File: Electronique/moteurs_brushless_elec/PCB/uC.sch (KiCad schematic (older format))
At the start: 17 parts, among them J1 CONN_SERIAL, J2 swdio, P1 CONN_I2C, P2 CONN_FREE, P3 CONN_CAN, U3 stm32f303k8t6, U9 MCP2562, Y1 Crystal_8MHz

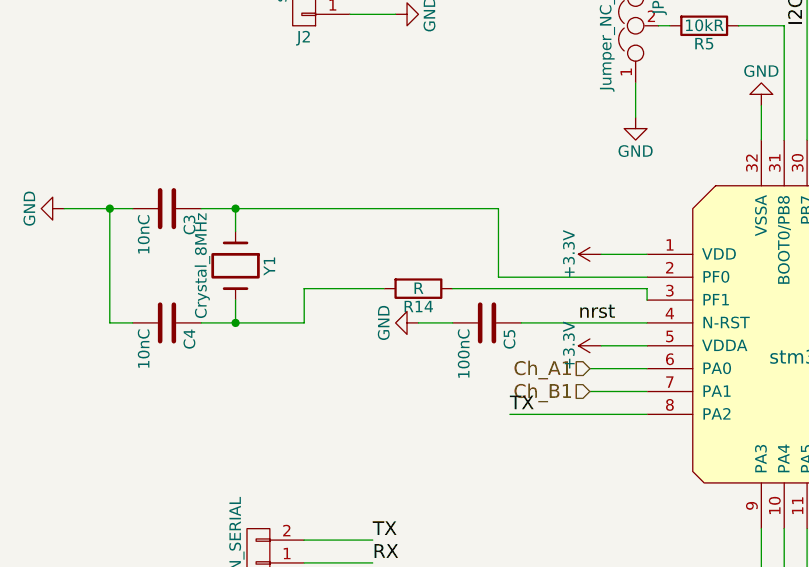
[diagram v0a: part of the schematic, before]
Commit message: pas de place pour le quartz
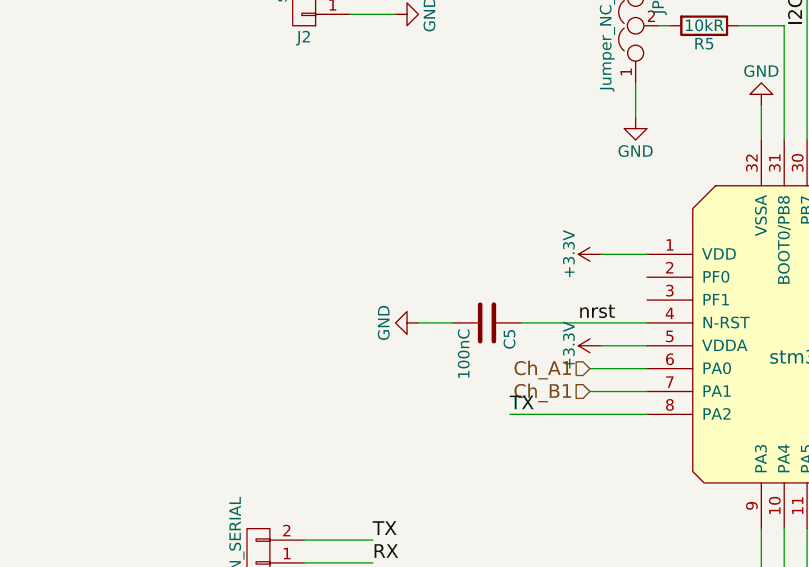
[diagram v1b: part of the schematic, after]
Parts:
- removed C3, C4: 10nC, Capacitors_SMD:C_1206_HandSoldering, symbol C
- removed R14: R, Resistors_SMD:R_1206_HandSoldering, symbol R
- removed Y1: Crystal_8MHz, Crystals:Crystal_HC49-4H_Vertical, symbol Crystal
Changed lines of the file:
@@
 I2C_SCL
-$Comp
-L Crystal Y1
-U 1 1 59C158A8
-P 3150 2750
-F 0 "Y1" H 3150 2900 50  0000 C CNN
-F 1 "Crystal_8MHz" H 3150 2600 50  0000 C CNN
-F 2 "Crystals:Crystal_HC49-4H_Vertical" H 3150 2750 50  0001 C CNN
-F 3 "" H 3150 2750 50  0000 C CNN
-	1    3150 2750
-	0    1    1    0
-$EndComp
-$Comp
-L C C3
-U 1 1 59C15931
-P 2850 2500
-F 0 "C3" H 2875 2600 50  0000 L CNN
-F 1 "10nC" H 2875 2400 50  0000 L CNN
-F 2 "Capacitors_SMD:C_1206_HandSoldering" H 2888 2350 50  0001 C CNN
-F 3 "" H 2850 2500 50  0000 C CNN
-	1    2850 2500
-	0    1    1    0
-$EndComp
-$Comp
-L C C4
-U 1 1 59C15C12
-P 2850 3000
-F 0 "C4" H 2875 3100 50  0000 L CNN
-F 1 "10nC" H 2875 2900 50  0000 L CNN
-F 2 "Capacitors_SMD:C_1206_HandSoldering" H 2888 2850 50  0001 C CNN
-F 3 "" H 2850 3000 50  0000 C CNN
-	1    2850 3000
-	0    1    1    0
-$EndComp
-$Comp
-L GND #PWR038
-U 1 1 59C15C7D
-P 2400 2500
-F 0 "#PWR038" H 2400 2250 50  0001 C CNN
-F 1 "GND" H 2400 2350 50  0000 C CNN
-F 2 "" H 2400 2500 50  0000 C CNN
-F 3 "" H 2400 2500 50  0000 C CNN
-	1    2400 2500
-	0    1    1    0
-$EndComp
-Wire Wire Line
-	2400 2500 2700 2500
-Wire Wire Line
-	2700 3000 2600 3000
-Wire Wire Line
-	2600 3000 2600 2500
-Connection ~ 2600 2500
-Wire Wire Line
-	3000 2500 4300 2500
-Wire Wire Line
-	3150 2500 3150 2600
-Wire Wire Line
-	3000 3000 3450 3000
-Wire Wire Line
-	3150 3000 3150 2900
-Connection ~ 3150 2500
-Connection ~ 3150 3000
 $Comp
 L CONN_01X02 P2
@@
 	5650 3900 5650 4550
 $Comp
-L R R14
-U 1 1 59C17650
-P 3950 2850
-F 0 "R14" V 4030 2850 50  0000 C CNN
-F 1 "R" V 3950 2850 50  0000 C CNN
-F 2 "Resistors_SMD:R_1206_HandSoldering" V 3880 2850 50  0001 C CNN
-F 3 "" H 3950 2850 50  0000 C CNN
-	1    3950 2850
-	0    1    1    0
-$EndComp
-Wire Wire Line
-	4100 2850 4950 2850
-Wire Wire Line
-	4950 2850 4950 2900
-Wire Wire Line
-	3800 2850 3450 2850
-Wire Wire Line
-	3450 2850 3450 3000
-Wire Wire Line
-	4300 2500 4300 2800
-Wire Wire Line
-	4300 2800 4950 2800
-$Comp
 L MCP2562 U9

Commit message: correction
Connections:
- no-connect marks 0 -> 2
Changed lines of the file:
@@
 $EndComp
 $Comp
-L +3.3V #PWR039
+L +3.3V #PWR038
 U 1 1 59C2F346
 P 3300 4500
-F 0 "#PWR039" H 3300 4350 50  0001 C CNN
+F 0 "#PWR038" H 3300 4350 50  0001 C CNN
 F 1 "+3.3V" H 3300 4640 50  0000 C CNN
 F 2 "" H 3300 4500 50  0000 C CNN
@@
 $EndComp
 $Comp
-L +5V #PWR040
+L +5V #PWR039
 U 1 1 59C2F5FE
 P 3700 4500
-F 0 "#PWR040" H 3700 4350 50  0001 C CNN
+F 0 "#PWR039" H 3700 4350 50  0001 C CNN
 F 1 "+5V" H 3700 4640 50  0000 C CNN
 F 2 "" H 3700 4500 50  0000 C CNN
@@
 $EndComp
 $Comp
-L GND #PWR041
+L GND #PWR040
 U 1 1 59C2F720
 P 3500 6100
-F 0 "#PWR041" H 3500 5850 50  0001 C CNN
+F 0 "#PWR040" H 3500 5850 50  0001 C CNN
 F 1 "GND" H 3500 5950 50  0000 C CNN
 F 2 "" H 3500 6100 50  0000 C CNN
@@
 $EndComp
 $Comp
-L GND #PWR042
+L GND #PWR041
 U 1 1 59C2F752
 P 2550 5650
-F 0 "#PWR042" H 2550 5400 50  0001 C CNN
+F 0 "#PWR041" H 2550 5400 50  0001 C CNN
 F 1 "GND" H 2550 5500 50  0000 C CNN
 F 2 "" H 2550 5650 50  0000 C CNN
@@
 	4650 5100 4650 5300
 Connection ~ 4450 5100
+NoConn ~ 4950 2800
+NoConn ~ 4950 2900
 $EndSCHEMATC

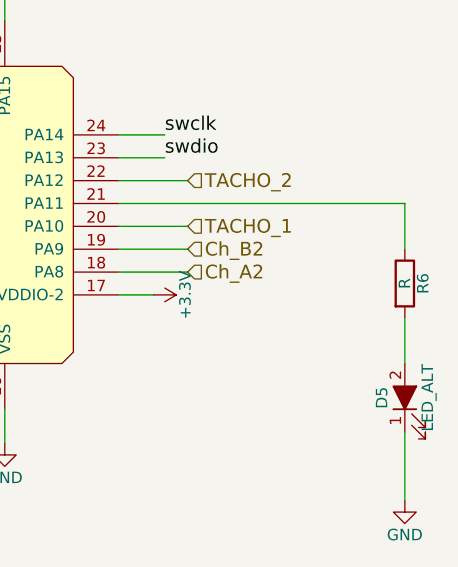
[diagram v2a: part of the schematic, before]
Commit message: modif moteur axe z
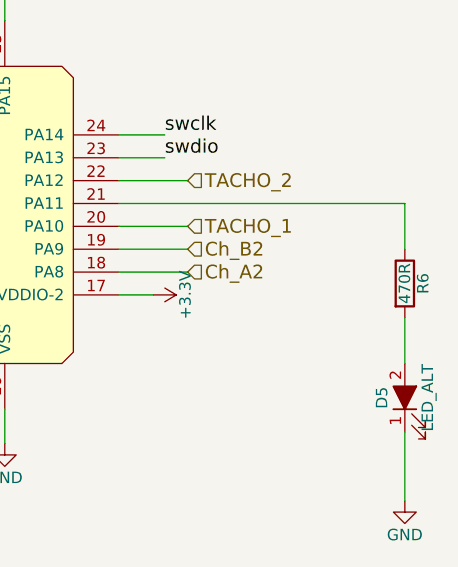
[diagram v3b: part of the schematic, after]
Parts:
- R6: value R -> 470R
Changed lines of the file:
@@
 P 7900 3350
 F 0 "R6" V 7980 3350 50  0000 C CNN
-F 1 "R" V 7900 3350 50  0000 C CNN
+F 1 "470R" V 7900 3350 50  0000 C CNN
 F 2 "Resistors_SMD:R_1206_HandSoldering" V 7830 3350 50  0001 C CNN
 F 3 "" H 7900 3350 50  0001 C CNN

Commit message: modif pour la commande
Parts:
- J2: footprint Pin_Headers:Pin_Header_Angled_1x04_Pitch2.54mm -> Pin_Headers:Pin_Header_Straight_1x04_Pitch2.54mm
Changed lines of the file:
@@
 F 0 "J2" H 3450 1750 50  0000 C CNN
 F 1 "swdio" V 3550 1500 50  0000 C CNN
-F 2 "Pin_Headers:Pin_Header_Angled_1x04_Pitch2.54mm" H 3450 1500 50  0001 C CNN
+F 2 "Pin_Headers:Pin_Header_Straight_1x04_Pitch2.54mm" H 3450 1500 50  0001 C CNN
 F 3 "" H 3450 1500 50  0001 C CNN
 	1    3450 1500

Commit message: ajout valeurs
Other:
- note added: "Pas utilisé"
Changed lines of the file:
@@
 NoConn ~ 4950 2800
 NoConn ~ 4950 2900
+Text Notes 4150 5800 0    60   ~ 0
+Pas utilisé
 $EndSCHEMATC
